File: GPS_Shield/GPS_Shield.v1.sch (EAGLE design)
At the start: 9 parts, among them T1 2N2222, U1 USD-SOCKETMOLEX-CORRECT

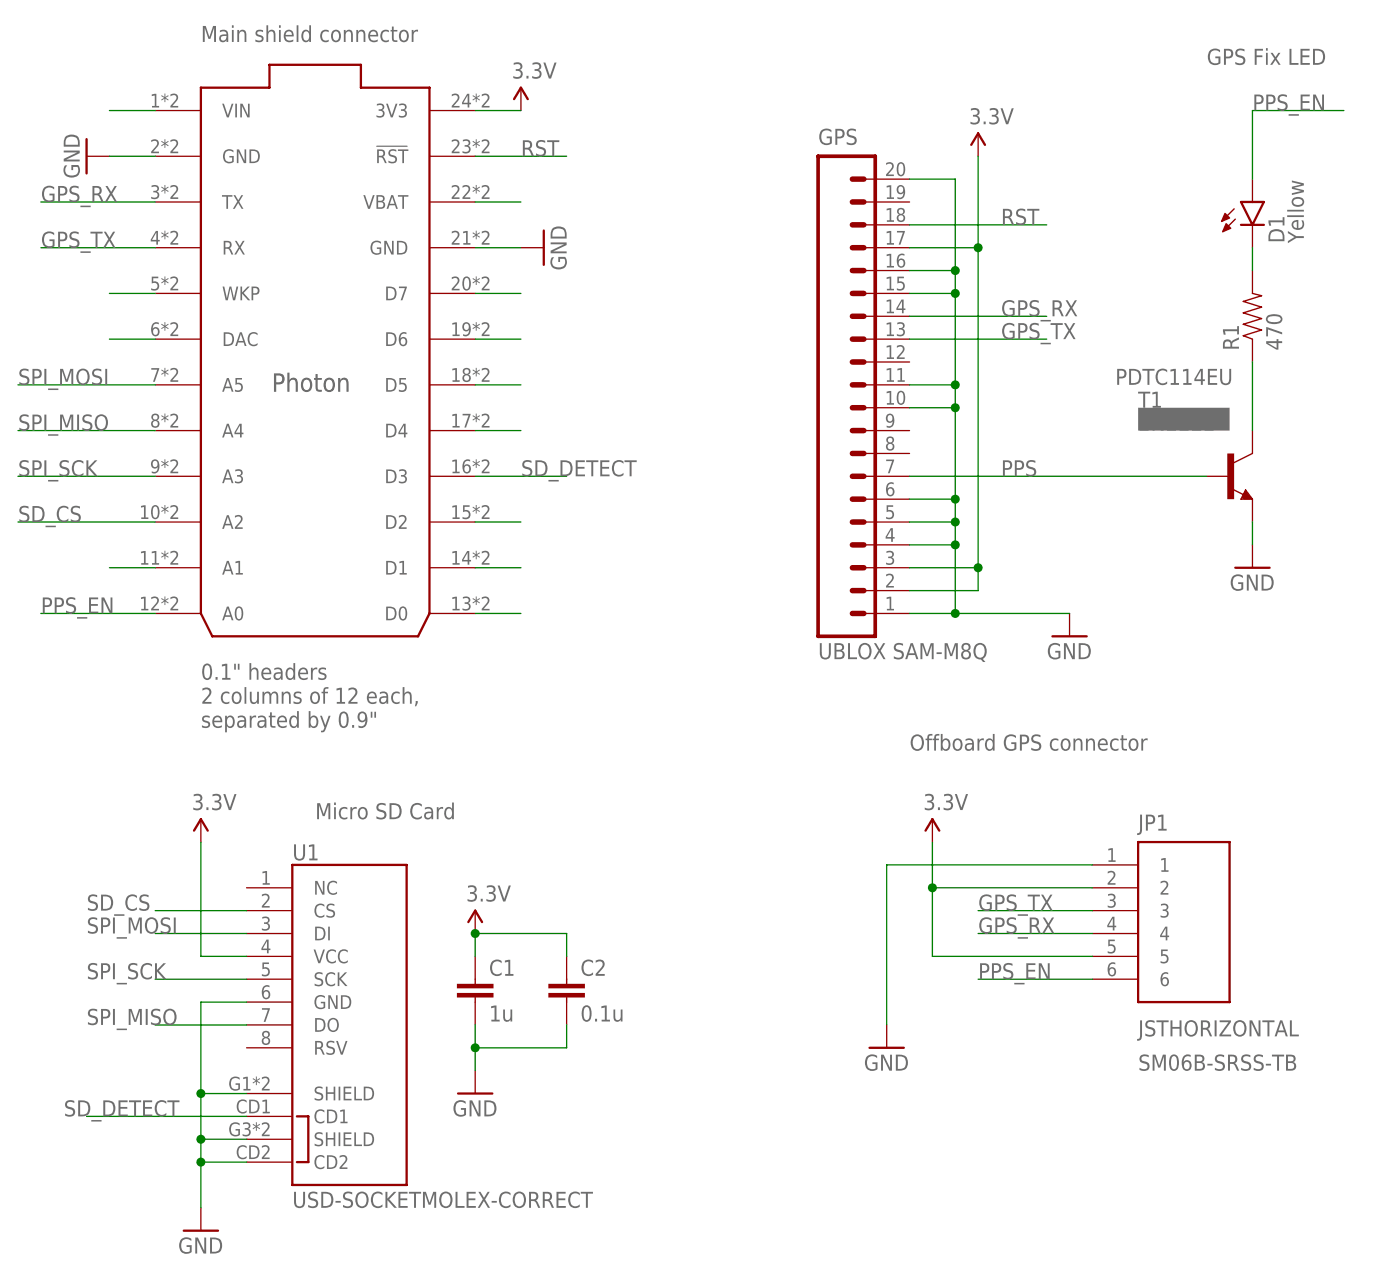
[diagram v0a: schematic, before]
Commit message: Add GPS_EN
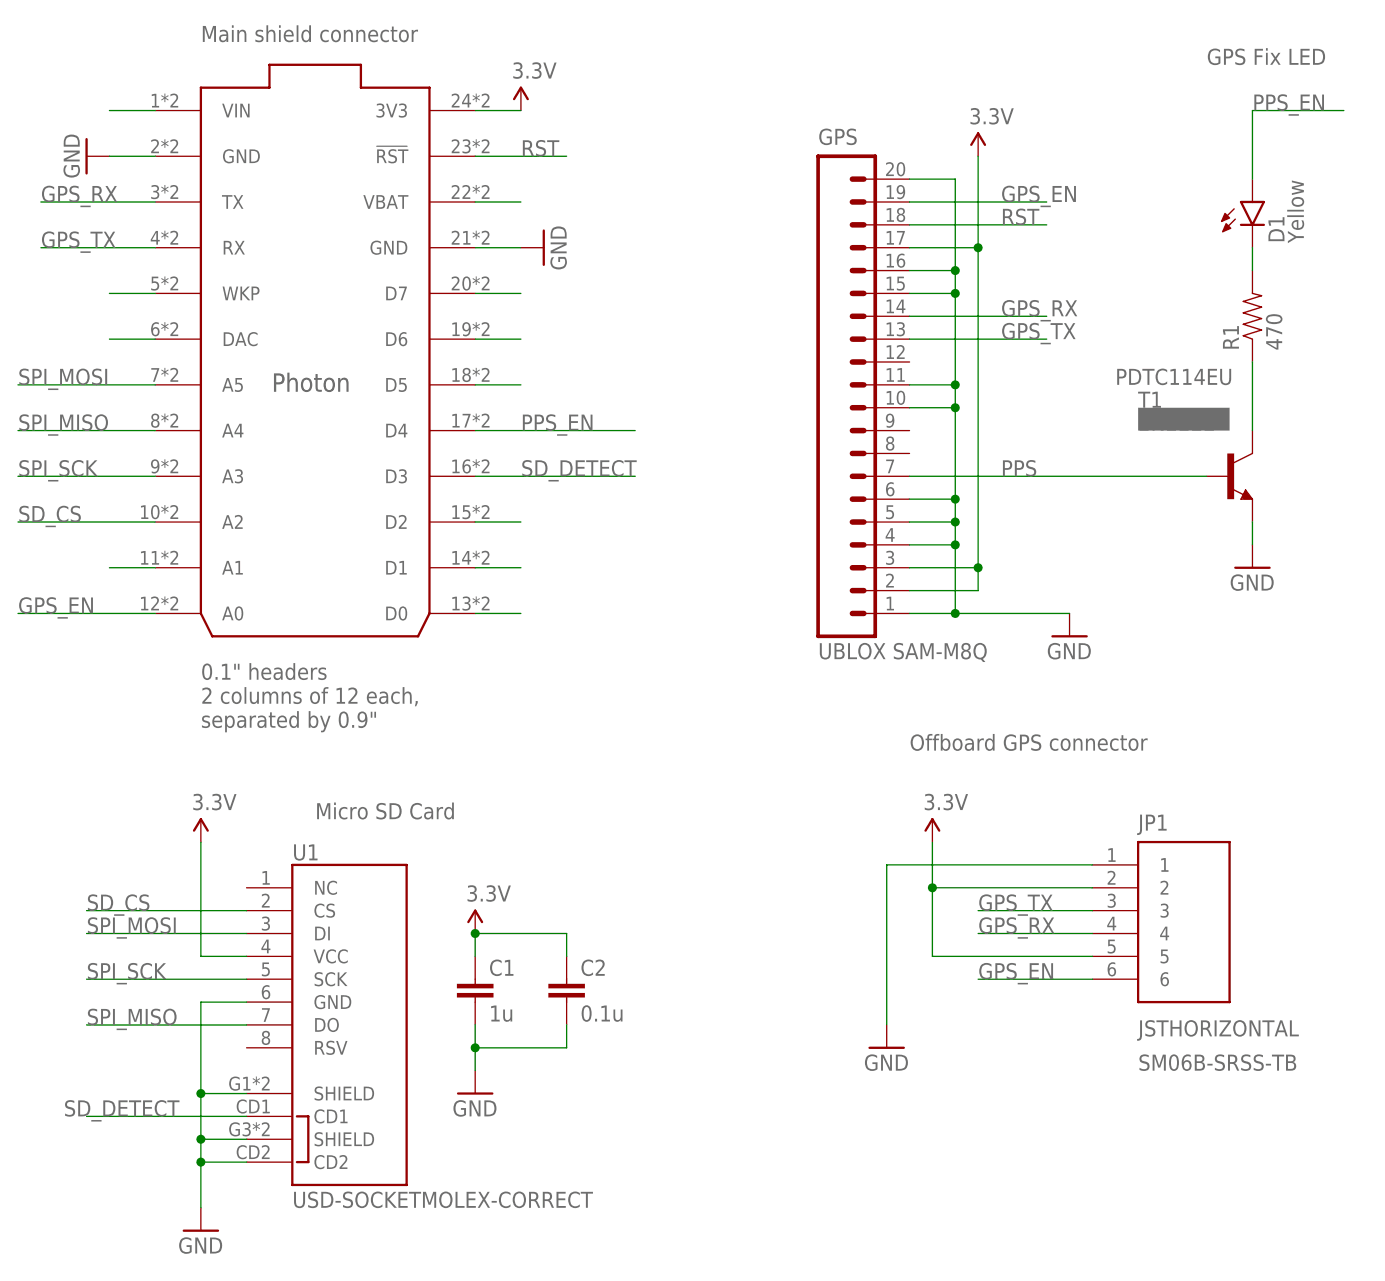
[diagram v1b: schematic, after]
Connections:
- removed net N$14: CORE.D5
- removed net N$15: CORE.D4
- new net GPS_EN: CORE.A0, GPS.19, JP1.6
- net PPS_EN: now also CORE.D4, CORE.D5; no longer CORE.A0, JP1.6
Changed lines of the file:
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@@
-</segment>
-</net>
-<net name="N$14" class="0">
-<segment>
-<pinref part="CORE" gate="G$1" pin="D5"/>
-<wire x1="5.08" y1="116.84" x2="10.16" y2="116.84" width="0.1524" layer="91"/>
-</segment>
-</net>
-<net name="N$15" class="0">
-<segment>
-<pinref part="CORE" gate="G$1" pin="D4"/>
-<wire x1="5.08" y1="111.76" x2="10.16" y2="111.76" width="0.1524" layer="91"/>
 </segment>
 </net>
@@
 </segment>
 <segment>
-<pinref part="CORE" gate="G$1" pin="A0"/>
-<wire x1="-30.48" y1="91.44" x2="-43.18" y2="91.44" width="0.1524" layer="91"/>
-<label x="-43.18" y="91.44" size="1.778" layer="95"/>
+<pinref part="CORE" gate="G$1" pin="D5"/>
+<wire x1="5.08" y1="116.84" x2="10.16" y2="116.84" width="0.1524" layer="91"/>
 </segment>
 <segment>
-<pinref part="JP1" gate="G$1" pin="6"/>
-<wire x1="73.66" y1="50.8" x2="60.96" y2="50.8" width="0.1524" layer="91"/>
-<label x="60.96" y="50.8" size="1.778" layer="95"/>
+<pinref part="CORE" gate="G$1" pin="D4"/>
+<wire x1="5.08" y1="111.76" x2="22.86" y2="111.76" width="0.1524" layer="91"/>
+<label x="10.16" y="111.76" size="1.778" layer="95"/>
 </segment>
 </net>
@@
 <segment>
 <pinref part="U1" gate="G$1" pin="CS"/>
-<wire x1="-20.32" y1="58.42" x2="-30.48" y2="58.42" width="0.1524" layer="91"/>
+<wire x1="-20.32" y1="58.42" x2="-38.1" y2="58.42" width="0.1524" layer="91"/>
 <label x="-38.1" y="58.42" size="1.778" layer="95"/>
 </segment>
@@
 <segment>
 <pinref part="U1" gate="G$1" pin="DI"/>
-<wire x1="-20.32" y1="55.88" x2="-30.48" y2="55.88" width="0.1524" layer="91"/>
+<wire x1="-20.32" y1="55.88" x2="-38.1" y2="55.88" width="0.1524" layer="91"/>
 <label x="-38.1" y="55.88" size="1.778" layer="95"/>
 </segment>
@@
 <segment>
 <pinref part="U1" gate="G$1" pin="SCK"/>
-<wire x1="-20.32" y1="50.8" x2="-30.48" y2="50.8" width="0.1524" layer="91"/>
+<wire x1="-20.32" y1="50.8" x2="-38.1" y2="50.8" width="0.1524" layer="91"/>
 <label x="-38.1" y="50.8" size="1.778" layer="95"/>
 </segment>
@@
 <segment>
 <pinref part="U1" gate="G$1" pin="DO"/>
-<wire x1="-20.32" y1="45.72" x2="-30.48" y2="45.72" width="0.1524" layer="91"/>
+<wire x1="-20.32" y1="45.72" x2="-38.1" y2="45.72" width="0.1524" layer="91"/>
 <label x="-38.1" y="45.72" size="1.778" layer="95"/>
 </segment>
@@
 <segment>
 <pinref part="CORE" gate="G$1" pin="D3"/>
-<wire x1="5.08" y1="106.68" x2="15.24" y2="106.68" width="0.1524" layer="91"/>
+<wire x1="5.08" y1="106.68" x2="22.86" y2="106.68" width="0.1524" layer="91"/>
 <label x="10.16" y="106.68" size="1.778" layer="95"/>
 </segment>
@@
 </segment>
 </net>
+<net name="GPS_EN" class="0">
+<segment>
+<pinref part="CORE" gate="G$1" pin="A0"/>
+<wire x1="-30.48" y1="91.44" x2="-45.72" y2="91.44" width="0.1524" layer="91"/>
+<label x="-45.72" y="91.44" size="1.778" layer="95"/>
+</segment>
+<segment>
+<pinref part="JP1" gate="G$1" pin="6"/>
+<wire x1="73.66" y1="50.8" x2="60.96" y2="50.8" width="0.1524" layer="91"/>
+<label x="60.96" y="50.8" size="1.778" layer="95"/>
+</segment>
+<segment>
+<pinref part="GPS" gate="G$1" pin="19"/>
+<wire x1="53.34" y1="137.16" x2="68.58" y2="137.16" width="0.1524" layer="91"/>
+<label x="63.5" y="137.16" size="1.778" layer="95"/>
+</segment>
+</net>

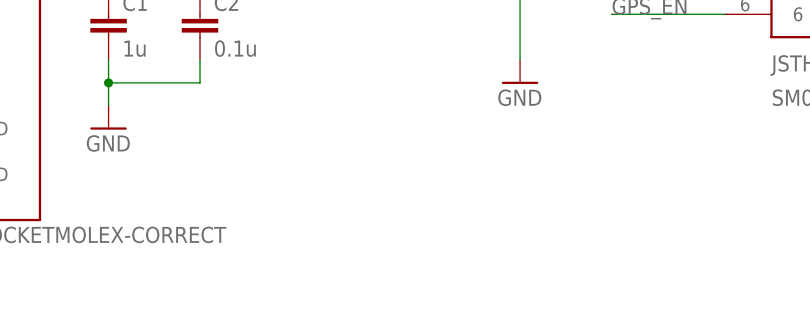
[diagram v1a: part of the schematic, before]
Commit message: Tweaks for silkscreen
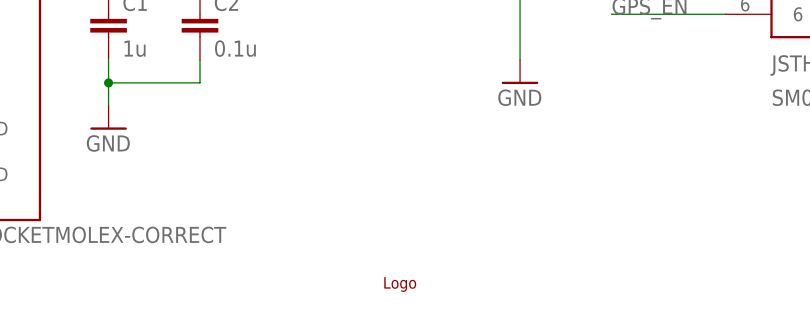
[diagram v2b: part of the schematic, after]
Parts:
- added U$1: LOGO, MuniRent:LOGO
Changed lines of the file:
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@@
 <part name="P+2" library="SparkFun-Aesthetics" deviceset="3.3V" device=""/>
 <part name="GND7" library="SparkFun-Aesthetics" deviceset="GND" device=""/>
+<part name="U$1" library="MuniRent" deviceset="LOGO" device=""/>
 </parts>
 <sheets>
@@
 <instance part="P+2" gate="G$1" x="10.16" y="147.32"/>
 <instance part="GND7" gate="1" x="12.7" y="132.08" rot="R90"/>
+<instance part="U$1" gate="G$1" x="35.56" y="20.32"/>
 </instances>
 <busses>
